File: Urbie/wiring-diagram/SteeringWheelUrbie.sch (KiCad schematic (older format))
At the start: 3 parts

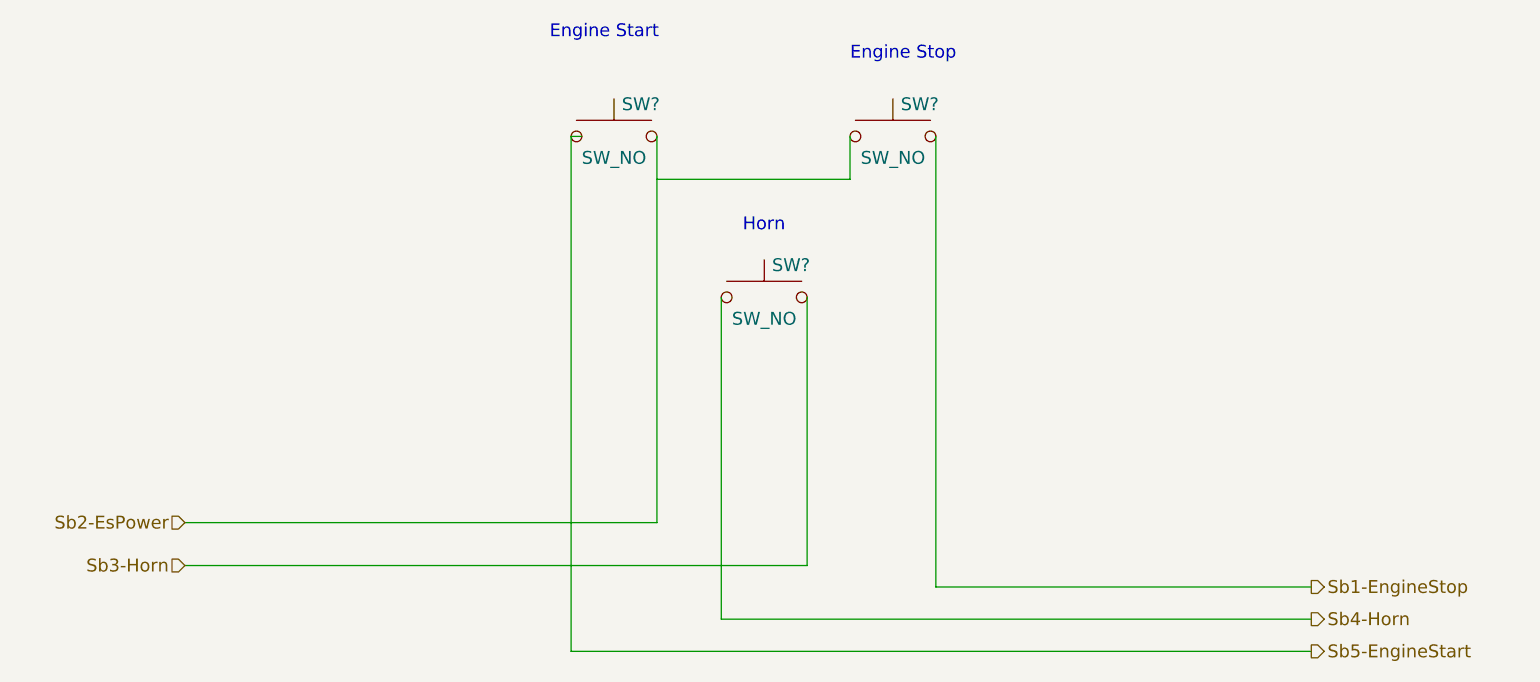
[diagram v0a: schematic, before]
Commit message: cleaning up schematics
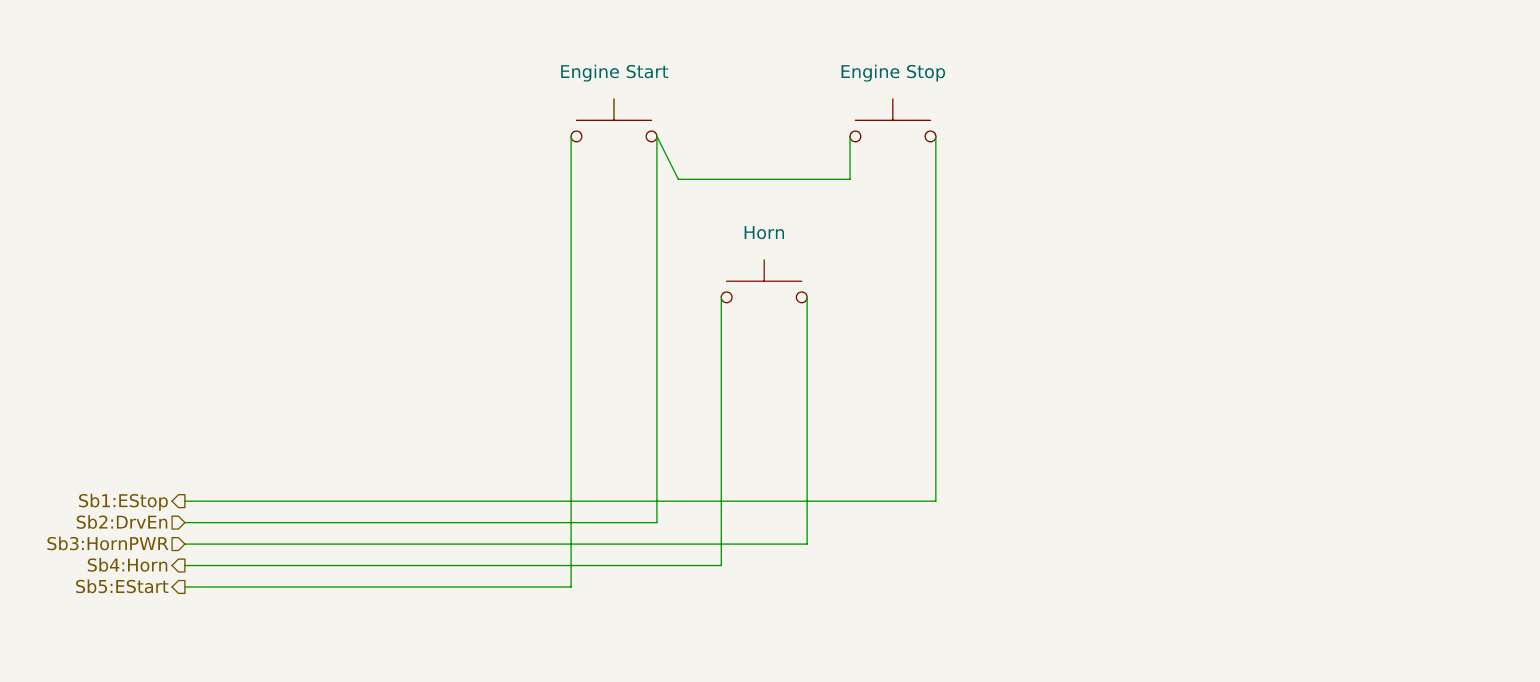
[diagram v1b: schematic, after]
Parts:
- SW?: value SW_NO -> Engine Start
- SW?: value SW_NO -> Engine Stop
- SW?: value SW_NO -> Horn
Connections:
- net labels added: Sb1:EStop, Sb2:DrvEn, Sb3:HornPWR, Sb4:Horn, Sb5:EStart
- net labels removed: Sb1-EngineStop, Sb2-EsPower, Sb3-Horn, Sb4-Horn, Sb5-EngineStart
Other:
- note removed: "Engine Start"
- note removed: "Engine Stop"
- note removed: "Horn"
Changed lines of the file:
@@
 U 1 1 57EFE3D4
 P 3750 2350
-F 0 "SW?" H 3875 2500 60  0000 C CNN
-F 1 "SW_NO" H 3750 2250 60  0000 C CNN
+F 0 "SW?" H 3875 2500 60  0001 C CNN
+F 1 "Engine Start" H 3750 2650 60  0000 C CNN
 F 2 "" H 3750 2350 60  0000 C CNN
 F 3 "" H 3750 2350 60  0000 C CNN
@@
 U 1 1 57EFE3F8
 P 5050 2350
-F 0 "SW?" H 5175 2500 60  0000 C CNN
-F 1 "SW_NO" H 5050 2250 60  0000 C CNN
+F 0 "SW?" H 5175 2500 60  0001 C CNN
+F 1 "Engine Stop" H 5050 2650 60  0000 C CNN
 F 2 "" H 5050 2350 60  0000 C CNN
 F 3 "" H 5050 2350 60  0000 C CNN
@@
 U 1 1 57EFE423
 P 4450 3100
-F 0 "SW?" H 4575 3250 60  0000 C CNN
-F 1 "SW_NO" H 4450 3000 60  0000 C CNN
+F 0 "SW?" H 4575 3250 60  0001 C CNN
+F 1 "Horn" H 4450 3400 60  0000 C CNN
 F 2 "" H 4450 3100 60  0000 C CNN
 F 3 "" H 4450 3100 60  0000 C CNN
@@
 	1    0    0    -1
 $EndComp
-Text Notes 3450 1900 0    60   ~ 0
-Engine Start
-Text Notes 4850 2000 0    60   ~ 0
-Engine Stop
-Text Notes 4350 2800 0    60   ~ 0
-Horn
 Wire Wire Line
-	4850 2350 4850 2550
-Wire Wire Line
-	4850 2550 3950 2550
+	4850 2550 4850 2350
 Wire Wire Line
 	3950 2350 3950 4150
 Text HLabel 1750 4150 0    60   Input ~ 0
-Sb2-EsPower
-Text HLabel 1750 4350 0    60   Input ~ 0
-Sb3-Horn
-Text HLabel 7000 4450 2    60   Output ~ 0
-Sb1-EngineStop
-Text HLabel 7000 4600 2    60   Output ~ 0
-Sb4-Horn
-Text HLabel 7000 4750 2    60   Output ~ 0
-Sb5-EngineStart
+Sb2:DrvEn
+Text HLabel 1750 4250 0    60   Input ~ 0
+Sb3:HornPWR
+Text HLabel 1750 4050 0    60   Output ~ 0
+Sb1:EStop
+Text HLabel 1750 4350 0    60   Output ~ 0
+Sb4:Horn
+Text HLabel 1750 4450 0    60   Output ~ 0
+Sb5:EStart
 Wire Wire Line
-	7000 4750 3550 4750
+	3550 4450 3550 2350
 Wire Wire Line
-	3550 4750 3550 2350
+	4250 4350 4250 3100
 Wire Wire Line
-	3550 2350 3600 2350
+	5250 4050 5250 2350
 Wire Wire Line
-	7000 4600 4250 4600
+	4650 4250 4650 3100
 Wire Wire Line
-	4250 4600 4250 3100
-Wire Wire Line
-	7000 4450 5250 4450
-Wire Wire Line
-	5250 4450 5250 2350
-Wire Wire Line
-	4650 4350 4650 3100
-Wire Wire Line
-	1750 4350 4650 4350
+	1750 4250 4650 4250
 Wire Wire Line
 	3950 4150 1750 4150
+Wire Wire Line
+	4050 2550 4850 2550
+Wire Wire Line
+	4050 2550 3950 2350
+Wire Wire Line
+	5250 4050 1750 4050
+Wire Wire Line
+	4250 4350 1750 4350
+Wire Wire Line
+	3550 4450 1750 4450
 $EndSCHEMATC
